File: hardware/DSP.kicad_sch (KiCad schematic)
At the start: 1 part, among them IC2 ADAU1467WBCPZ300RL

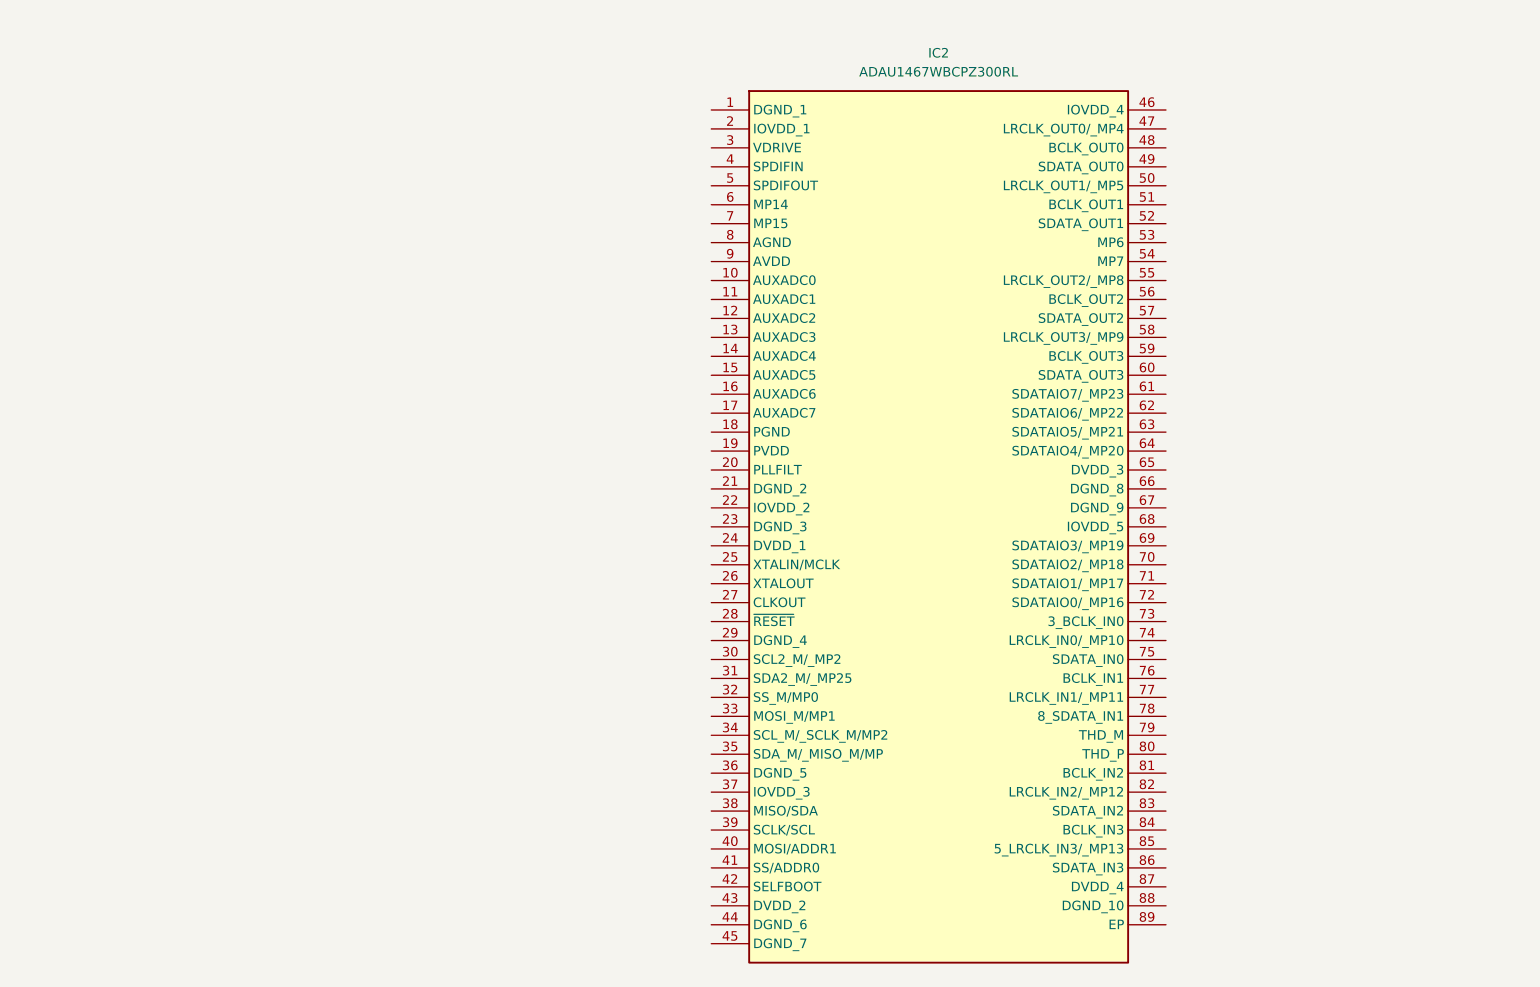
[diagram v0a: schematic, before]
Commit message: finished eARC and started with DSP
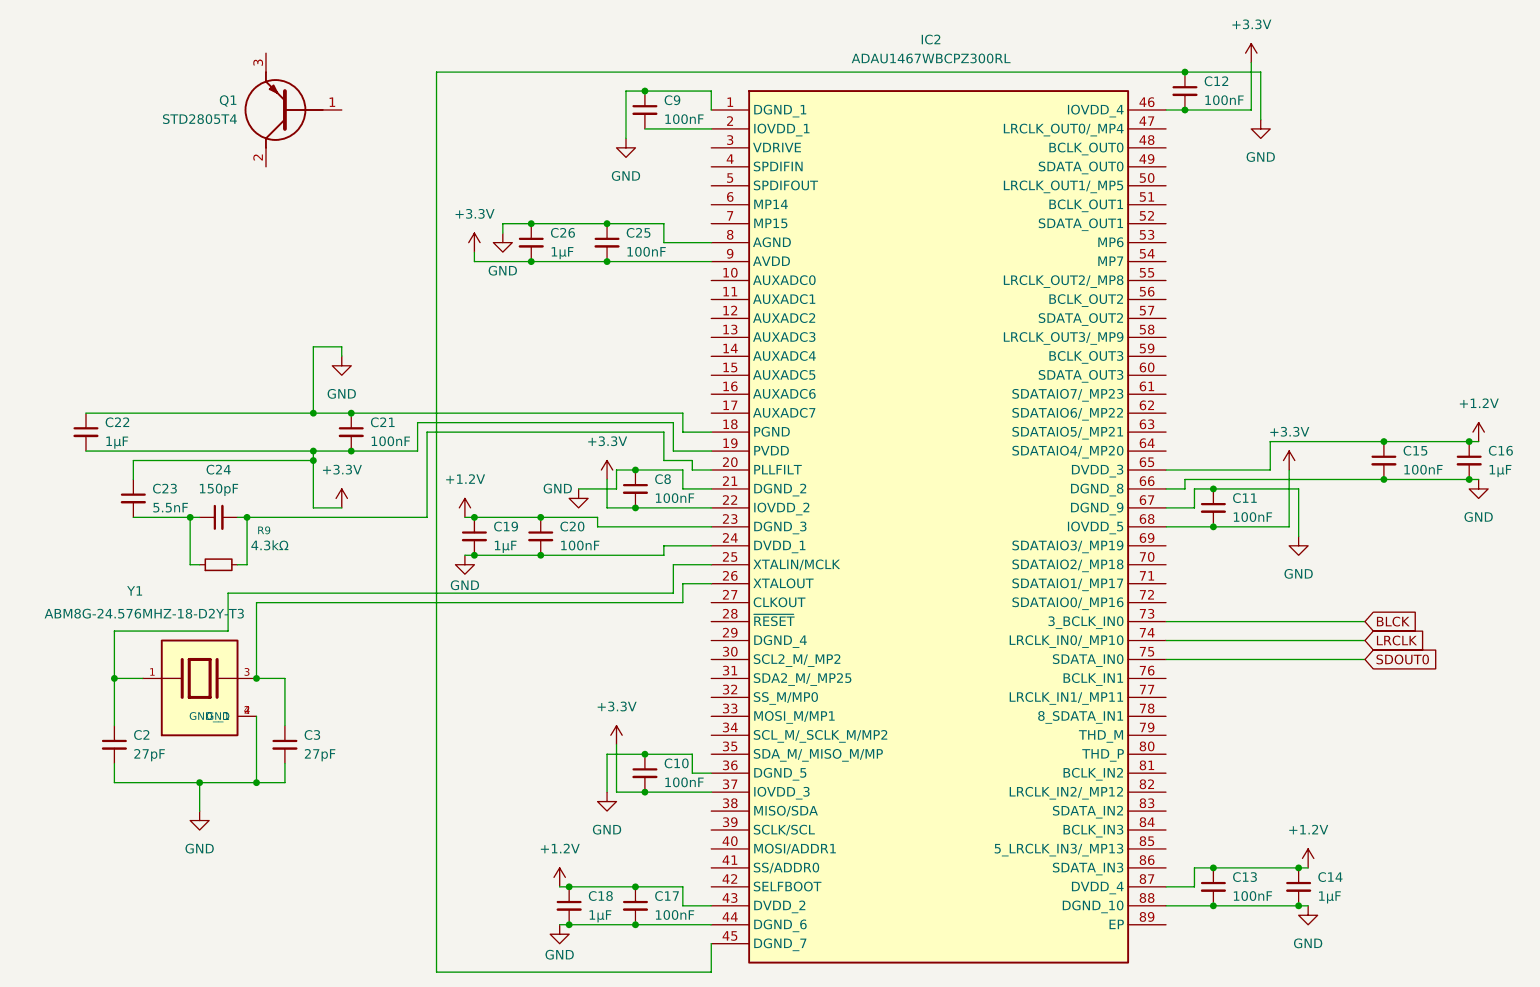
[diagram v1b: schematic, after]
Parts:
- added C10, C11, C12, C13, C15, C17, C20, C21, C25, C8, C9: 100nF, symbol Device:C_Small
- added C14, C16, C18, C19, C22, C26: 1μF, symbol Device:C_Small
- added C2, C3: 27pF, symbol Device:C_Small
- added C23: 5.5nF, symbol Device:C_Small
- added C24: 150pF, symbol Device:C_Small
- added Q1: STD2805T4, STD2805T4, symbol piavr:STD2805T4
- added R9: 4.3kΩ, symbol Device:R_Small
- added Y1: ABM8G-24.576MHZ-18-D2Y-T3, ABM8G-24.576MHZ-18-D2Y-T3:XTAL_ABM8G-24.576MHZ-18-D2Y-T3, symbol piavr:ABM8G-24.576MHZ-18-D2Y-T3
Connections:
- net GND: now reaches IC2.1 (DGND_1)
- net GND: now also IC2.18 (PGND), IC2.21 (DGND_2), IC2.24 (DVDD_1), IC2.36 (DGND_5), IC2.44 (DGND_6), IC2.45 (DGND_7), IC2.66 (DGND_8), IC2.67 (DGND_9), IC2.8 (AGND), IC2.88 (DGND_10), C10.1, C11.1, C12.1, C13.2, C14.2, C15.2, C16.2, C17.2, C18.2, C19.2, C2.2, C20.2, C21.1, C22.1, C25.1, C26.1, C3.2, C8.1, C9.1, Y1.2 (GND), Y1.4 (GND__1)
- net +3.3V: now reaches IC2.19 (PVDD)
- net +3.3V: now also IC2.22 (IOVDD_2), IC2.37 (IOVDD_3), IC2.46 (IOVDD_4), IC2.68 (IOVDD_5), IC2.9 (AVDD), C10.2, C11.2, C12.2, C21.2, C22.2, C23.1, C25.2, C26.2, C8.2
- net at IC2.2 (IOVDD_1): now also C9.2
- net at IC2.20 (PLLFILT): now also C24.2, R9.2
- net +1.2V: now reaches IC2.23 (DGND_3)
- net +1.2V: now also IC2.43 (DVDD_2), IC2.65 (DVDD_3), IC2.87 (DVDD_4), C13.1, C14.1, C15.1, C16.1, C17.1, C18.1, C19.1, C20.1
- net at IC2.25 (XTALIN/MCLK): now also C2.1, Y1.1
- net at IC2.26 (XTALOUT): now also C3.1, Y1.3
- net BLCK: now reaches IC2.73 (3_BCLK_IN0)
- net LRCLK: now reaches IC2.74 (LRCLK_IN0/_MP10)
- net SDOUT0: now reaches IC2.75 (SDATA_IN0)
- new net: C23.2, C24.1, R9.1
